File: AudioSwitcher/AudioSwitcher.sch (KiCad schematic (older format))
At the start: 18 parts

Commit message: Updated schematic
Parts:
- added C? (x6): C, symbol Device:C
- added J?: Conn_01x02_Male, symbol Connector:Conn_01x02_Male
- added SW?: Channel1Btn, symbol Switch:SW_Push_Dual
- added SW?: Channel2Btn, symbol Switch:SW_Push_Dual
- added SW?: Channel3Btn, symbol Switch:SW_Push_Dual
- added SW?: Channel4Btn, symbol Switch:SW_Push_Dual
- added SW?: PatchUpBtn, symbol Switch:SW_Push_Dual
- added SW?: PatchDownBtn, symbol Switch:SW_Push_Dual
- added SW?: ModeToggleBtn, symbol Switch:SW_Push_Dual
- added SW?: PatchSaveBtn, symbol Switch:SW_Push_Dual
- added SW?: BypassSwitch, symbol Switch:SW_Push_DPDT
- added U? (x4): 74HC595, symbol 74xx:74HC595
- added U?: 4051, symbol 4xxx:4051
- added U?: L7805, symbol Regulator_Linear:L7805
- added Y?: Crystal, symbol Device:Crystal
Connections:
- net GND: now also C?.2, C?.2, C?.2, C?.2, C?.2, C?.2, J?.2 (Pin_2), SW?.1, SW?.1, SW?.1, SW?.1, SW?.1, SW?.1, SW?.1, SW?.1, SW?.3, SW?.3, SW?.3, SW?.3, SW?.3, SW?.3, SW?.3, SW?.3, U?.10 (~SRCLR), U?.10 (~SRCLR), U?.10 (~SRCLR), U?.10 (~SRCLR), U?.7 (VEE), U?.8 (GND), U?.8 (GND), U?.8 (GND), U?.8 (GND), U?.8 (VSS)
- net Mux5_A: now also U?.1 (QB)
- net Mux5_B: now also U?.2 (QC)
- net Mux5_C: now also U?.3 (QD)
- net Mux5_Inh: now also U?.15 (QA)
- net ShiftRegClock: now also U?.11 (SRCLK)
- net ShiftRegLatch: now also U?.12 (RCLK)
- net +5V: now reaches U?.20 (AVCC)
- net +5V: now also U?.7 (VCC), C?.1, C?.1, U?.3 (OUT)
- net at U?.9 (QH'): now also U?.14 (SER)
- new net: U?.14 (SER), U?.9 (QH') (x2)
- new net: C?.1, C?.1, J?.1 (Pin_1), U?.1 (IN)
- new net BtnMuxA: U?.11 (A)
- new net BtnMuxB: U?.10 (B)
- new net BtnMuxC: U?.9 (C)
- new net BtnMuxOut: U?.3 (X)
- new net Channel1Btn: SW?.2, SW?.4, U?.13 (X0)
- new net Channel1Led: U?.15 (QA)
- new net Channel2Btn: SW?.2, SW?.4, U?.14 (X1)
- new net Channel2Led: U?.1 (QB)
- new net Channel3Btn: SW?.2, SW?.4, U?.15 (X2)
- new net Channel3Led: U?.2 (QC)
- new net Channel4Btn: SW?.2, SW?.4, U?.12 (X3)
- new net Channel4Led: U?.3 (QD)
- new net LEDShiftRegClock: U?.11 (SRCLK), U?.11 (SRCLK), U?.11 (SRCLK)
- new net LEDShiftRegData: U?.14 (SER)
- new net LEDShiftRegLatch: U?.12 (RCLK), U?.12 (RCLK), U?.12 (RCLK)
- new net ModeLed: U?.4 (QE)
- new net ModeToggleBtn: SW?.2, SW?.4, U?.2 (X6)
- new net PatchDownBtn: SW?.2, SW?.4, U?.5 (X5)
- new net PatchSaveBtn: SW?.2, SW?.4, U?.4 (X7)
- new net PatchUpBtn: SW?.2, SW?.4, U?.1 (X4)
- new net SevenSeg1A: U?.15 (QA)
- new net SevenSeg1B: U?.1 (QB)
- new net SevenSeg1C: U?.2 (QC)
- new net SevenSeg1D: U?.3 (QD)
- new net SevenSeg1E: U?.4 (QE)
- new net SevenSeg1F: U?.5 (QF)
- new net SevenSeg1G: U?.6 (QG)
- new net SevenSeg1H: U?.7 (QH)
- new net SevenSeg2A: U?.15 (QA)
- new net SevenSeg2B: U?.1 (QB)
- new net SevenSeg2C: U?.2 (QC)
- new net SevenSeg2D: U?.3 (QD)
- new net SevenSeg2E: U?.4 (QE)
- new net SevenSeg2F: U?.5 (QF)
- new net SevenSeg2G: U?.6 (QG)
- new net SevenSeg2H: U?.7 (QH)
- new net XtalA: C?.1, Y?.1
- new net XtalB: C?.1, Y?.2
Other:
- note added: "Button Mux"
- note added: "Buttons"
- note added: "IO Jacks\n"
- note added: "IO Muxes"
- note added: "IO Select Shift Registers"
- note added: "LED & Seven Segment Shift Registers"
- note added: "Microcontroller"
- note added: "Power Supply"
- moved on the sheet: J?, U?

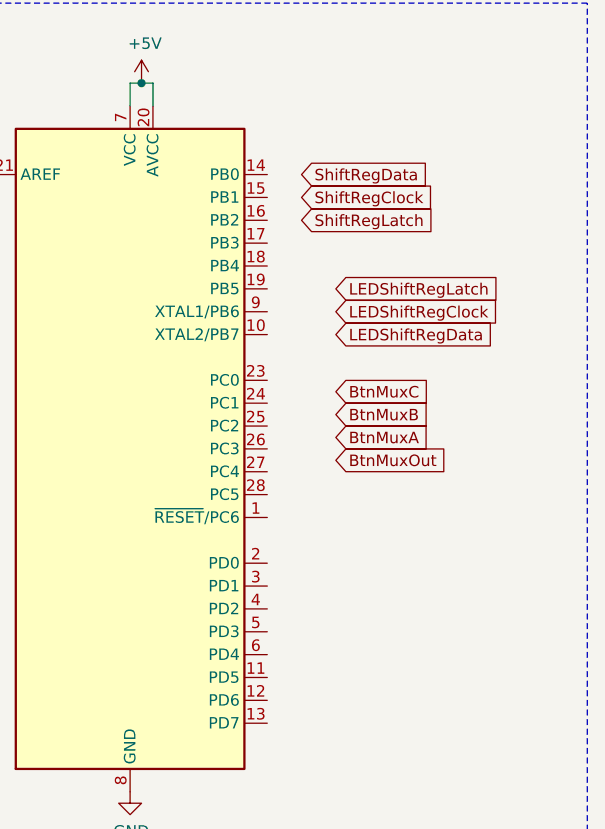
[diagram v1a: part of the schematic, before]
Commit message: Added peripheral labels
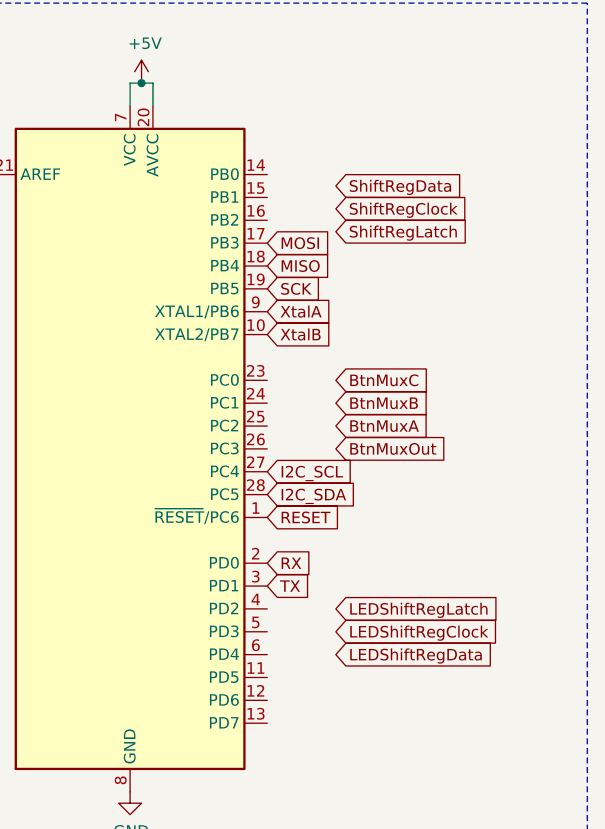
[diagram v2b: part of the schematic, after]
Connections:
- net XtalA: now also U?.9 (XTAL1/PB6)
- net XtalB: now also U?.10 (XTAL2/PB7)
- net RESET: now reaches U?.1 (~RESET~/PC6)
- net MOSI: now reaches U?.17 (PB3)
- net MISO: now reaches U?.18 (PB4)
- net SCK: now reaches U?.19 (PB5)
- net RX: now reaches U?.2 (PD0)
- net I2C_SCL: now reaches U?.27 (PC4)
- net I2C_SDA: now reaches U?.28 (PC5)
- net TX: now reaches U?.3 (PD1)
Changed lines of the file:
@@
 	1    0    0    -1
 $EndComp
-Text GLabel 14300 1500 2    50   Input ~ 0
+Text GLabel 14450 1550 2    50   Input ~ 0
 ShiftRegData
-Text GLabel 14300 1600 2    50   Input ~ 0
+Text GLabel 14450 1650 2    50   Input ~ 0
 ShiftRegClock
-Text GLabel 14300 1700 2    50   Input ~ 0
+Text GLabel 14450 1750 2    50   Input ~ 0
 ShiftRegLatch
 Text GLabel 1800 6750 0    50   Input ~ 0
@@
 Text GLabel 1750 9750 0    50   Input ~ 0
 LEDShiftRegLatch
-Text GLabel 14450 2100 2    50   Input ~ 0
+Text GLabel 14450 3500 2    50   Input ~ 0
 LEDShiftRegClock
-Text GLabel 14450 2200 2    50   Input ~ 0
+Text GLabel 14450 3600 2    50   Input ~ 0
 LEDShiftRegData
-Text GLabel 14450 2000 2    50   Input ~ 0
+Text GLabel 14450 3400 2    50   Input ~ 0
 LEDShiftRegLatch
 Text GLabel 1750 9550 0    50   Input ~ 0
@@
 	1    0    0    -1
 $EndComp
-Text GLabel 14450 2650 2    50   Input ~ 0
+Text GLabel 14450 2600 2    50   Input ~ 0
 BtnMuxA
-Text GLabel 14450 2550 2    50   Input ~ 0
+Text GLabel 14450 2500 2    50   Input ~ 0
 BtnMuxB
-Text GLabel 14450 2450 2    50   Input ~ 0
+Text GLabel 14450 2400 2    50   Input ~ 0
 BtnMuxC
 Text GLabel 10550 9000 2    50   Input ~ 0
 BtnMuxOut
-Text GLabel 14450 2750 2    50   Input ~ 0
+Text GLabel 14450 2700 2    50   Input ~ 0
 BtnMuxOut
 $Comp
@@
 Wire Notes Line
 	8600 6300 15200 6300
+Text GLabel 14150 3300 2    50   Input ~ 0
+TX
+Text GLabel 14150 3200 2    50   Input ~ 0
+RX
+Text GLabel 14150 2200 2    50   Input ~ 0
+XtalB
+Text GLabel 14150 2100 2    50   Input ~ 0
+XtalA
+Text GLabel 14150 2800 2    50   Input ~ 0
+I2C_SCL
+Text GLabel 14150 2900 2    50   Input ~ 0
+I2C_SDA
+Text GLabel 14150 2000 2    50   Input ~ 0
+SCK
+Text GLabel 14150 1800 2    50   Input ~ 0
+MOSI
+Text GLabel 14150 1900 2    50   Input ~ 0
+MISO
+Text GLabel 14150 3000 2    50   Input ~ 0
+RESET
 $EndSCHEMATC

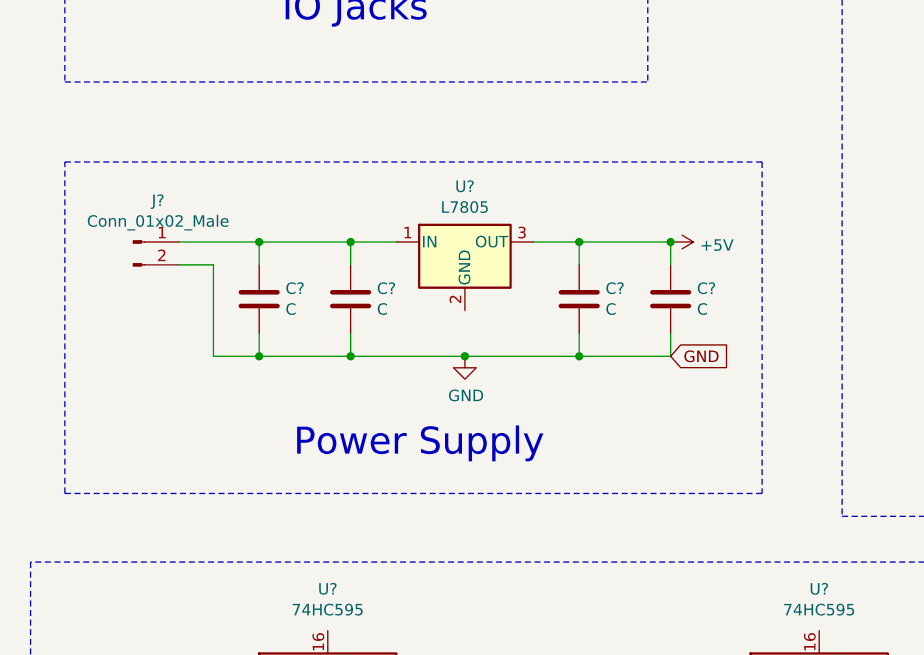
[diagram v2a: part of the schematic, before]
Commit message: Added reverse voltage protection
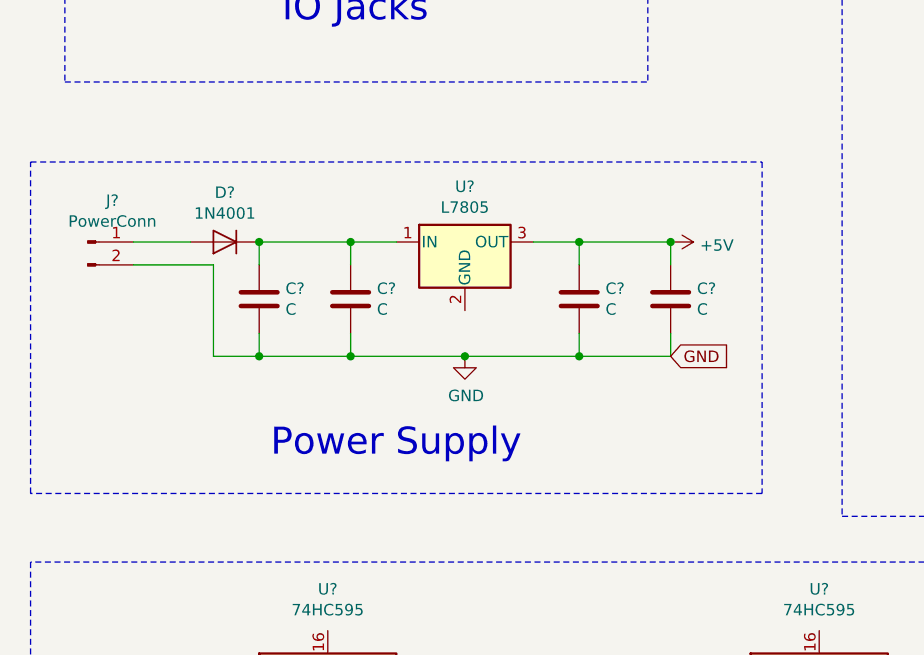
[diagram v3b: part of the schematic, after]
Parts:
- added D?: 1N4001, Diode_THT:D_DO-41_SOD81_P10.16mm_Horizontal, symbol Diode:1N4001
- J?: value Conn_01x02_Male -> PowerConn
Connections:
- net at C?.1, C?.1, U?.1 (IN): now also D?.1 (K); no longer J?.1 (Pin_1)
- new net: D?.2 (A), J?.1 (Pin_1)
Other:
- moved on the sheet: J?
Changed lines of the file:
@@
 $EndComp
 Connection ~ 3700 4850
-Text Notes 2050 5800 0    118  ~ 0
+Text Notes 1950 5800 0    118  ~ 0
 Power Supply
 Wire Notes Line
@@
 L Connector:Conn_01x02_Male J?
 U 1 1 6157BF67
-P 1350 4850
-F 0 "J?" H 1458 5031 50  0000 C CNN
-F 1 "Conn_01x02_Male" H 1458 4940 50  0000 C CNN
-F 2 "" H 1350 4850 50  0001 C CNN
-F 3 "~" H 1350 4850 50  0001 C CNN
-	1    1350 4850
+P 1150 4850
+F 0 "J?" H 1258 5031 50  0000 C CNN
+F 1 "PowerConn" H 1258 4940 50  0000 C CNN
+F 2 "" H 1150 4850 50  0001 C CNN
+F 3 "~" H 1150 4850 50  0001 C CNN
+	1    1150 4850
 	1    0    0    -1
 $EndComp
-Wire Wire Line
-	1550 4850 1900 4850
-Connection ~ 1900 4850
 Wire Wire Line
 	1900 5350 1700 5350
 Wire Wire Line
 	1700 5350 1700 4950
-Wire Wire Line
-	1700 4950 1550 4950
 Connection ~ 1900 5350
-Wire Notes Line
-	1050 4500 4100 4500
 Wire Notes Line
 	4100 4500 4100 5950
 Wire Notes Line
-	4100 5950 1050 5950
-Wire Notes Line
-	1050 5950 1050 4500
+	900  5950 900  4500
 Wire Notes Line
 	4450 850  4450 6050
@@
 Text GLabel 14150 3000 2    50   Input ~ 0
 RESET
+$Comp
+L Diode:1N4001 D?
+U 1 1 6171DF28
+P 1750 4850
+F 0 "D?" H 1750 4634 50  0000 C CNN
+F 1 "1N4001" H 1750 4725 50  0000 C CNN
+F 2 "Diode_THT:D_DO-41_SOD81_P10.16mm_Horizontal" H 1750 4675 50  0001 C CNN
+F 3 "http://www.vishay.com/docs/88503/1n4001.pdf" H 1750 4850 50  0001 C CNN
+	1    1750 4850
+	-1   0    0    1
+$EndComp
+Connection ~ 1900 4850
+Wire Wire Line
+	1600 4850 1350 4850
+Wire Wire Line
+	1350 4950 1700 4950
+Wire Notes Line
+	900  4500 4100 4500
+Wire Notes Line
+	4100 5950 900  5950
 $EndSCHEMATC

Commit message: Added comments
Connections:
- net GND: now also U?.2 (GND)
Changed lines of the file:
@@
 Wire Notes Line
 	4100 5950 900  5950
+Wire Wire Line
+	2800 5150 2800 5350
 $EndSCHEMATC
